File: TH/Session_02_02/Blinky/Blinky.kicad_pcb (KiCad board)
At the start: 2 copper layers, 12 parts, among them U1 TLC551CD‎

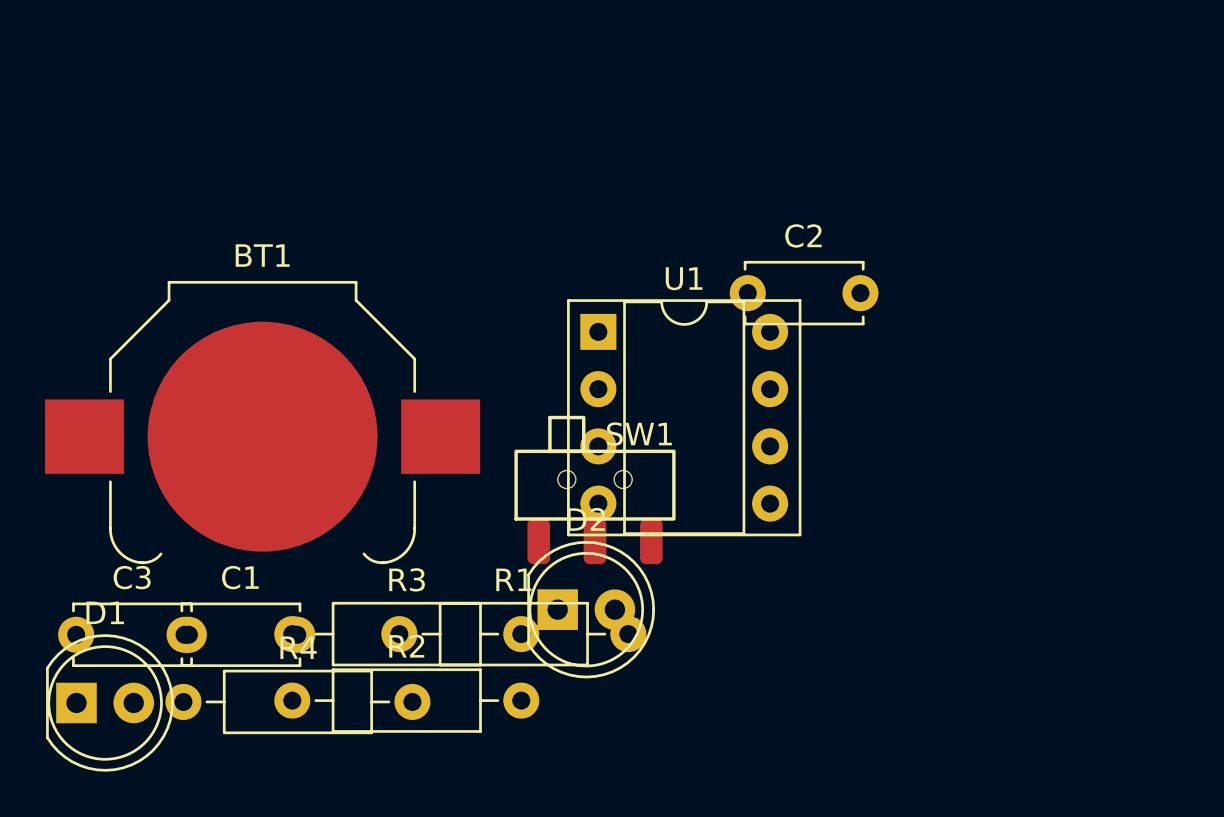
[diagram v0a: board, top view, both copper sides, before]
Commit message: Revamps the through-hole project as transistor based
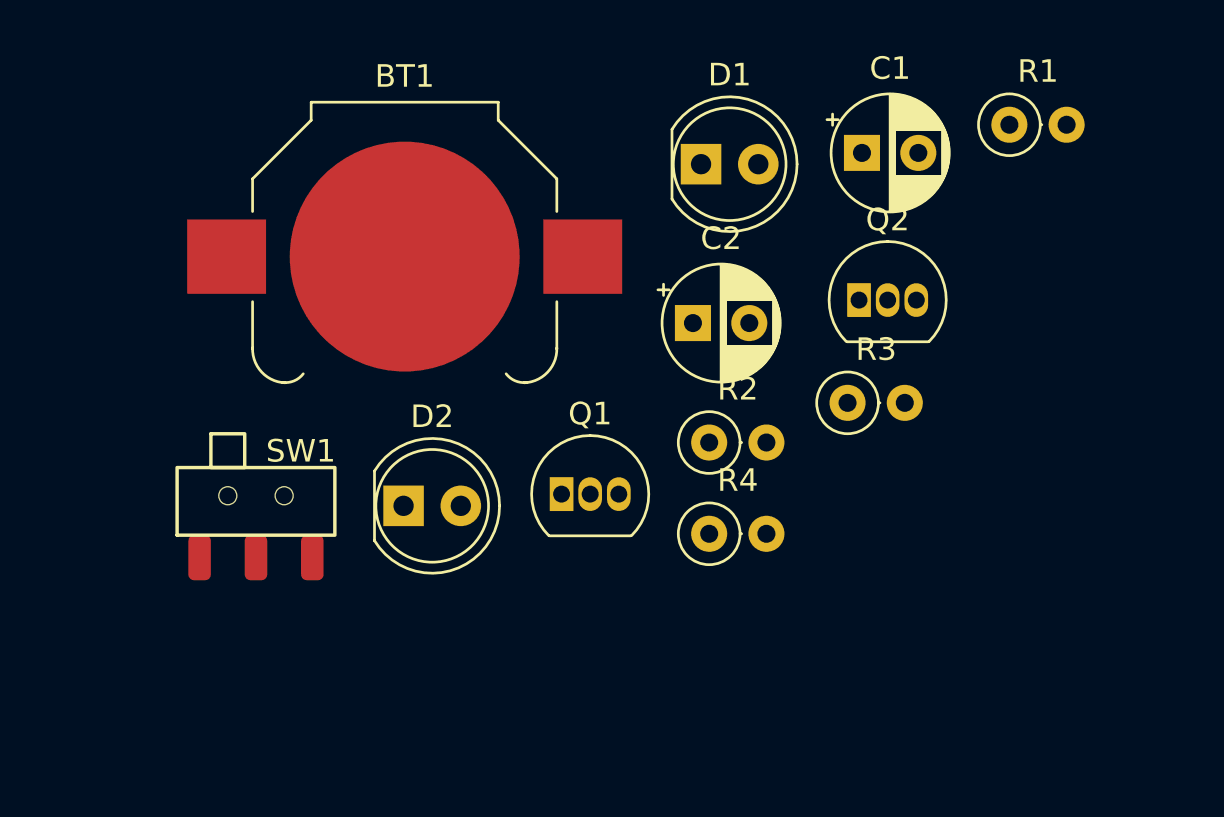
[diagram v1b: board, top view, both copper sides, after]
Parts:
- removed C3: 100nF, Capacitor_THT:C_Disc_D5.0mm_W2.5mm_P5.00mm
- removed SW?: SW_SPDT, Blinky_ZAM:SSK-1202
- removed U1: TLC551CD‎, Package_DIP:DIP-8_W7.62mm_Socket
- added Q1: 2N3904, Package_TO_SOT_THT:TO-92_Inline, F.Cu at (155.0, 98.4)
- added Q2: 2N3904, Package_TO_SOT_THT:TO-92_Inline, F.Cu at (168.2, 89.8)
- added SW1: SW_SPST, Blinky_ZAM:SSK-1202, F.Cu at (141.5, 101.2)
- C1: value 300nF -> 10μF; footprint Capacitor_THT:C_Disc_D5.0mm_W2.5mm_P5.00mm -> Capacitor_THT:CP_Radial_D5.0mm_P2.50mm
- C2: value 100nF -> 10μF; footprint Capacitor_THT:C_Disc_D5.0mm_W2.5mm_P5.00mm -> Capacitor_THT:CP_Radial_D5.0mm_P2.50mm
- R1: value 10kΩ -> 220Ω; footprint Resistor_THT:R_Axial_DIN0207_L6.3mm_D2.5mm_P10.16mm_Horizontal -> Resistor_THT:R_Axial_DIN0207_L6.3mm_D2.5mm_P2.54mm_Vertical
- R2: value 1MΩ -> 100kΩ; footprint Resistor_THT:R_Axial_DIN0207_L6.3mm_D2.5mm_P10.16mm_Horizontal -> Resistor_THT:R_Axial_DIN0207_L6.3mm_D2.5mm_P2.54mm_Vertical
- R3: value 200Ω -> 100kΩ; footprint Resistor_THT:R_Axial_DIN0207_L6.3mm_D2.5mm_P10.16mm_Horizontal -> Resistor_THT:R_Axial_DIN0207_L6.3mm_D2.5mm_P2.54mm_Vertical
- R4: value 200Ω -> 220Ω; footprint Resistor_THT:R_Axial_DIN0207_L6.3mm_D2.5mm_P10.16mm_Horizontal -> Resistor_THT:R_Axial_DIN0207_L6.3mm_D2.5mm_P2.54mm_Vertical
- moved C1 36.9 mm to (168.4, 83.3)
- moved D1 36.6 mm to (161.2, 83.8)
- moved R1 35.3 mm to (174.9, 82.0)
- moved R3 26.7 mm to (167.7, 94.4)
- moved R4 24.5 mm to (161.6, 100.2)
- moved R2 21.8 mm to (161.6, 96.1)
- moved BT1 10.2 mm to (148.1, 87.9)
- moved D2 8.24 mm to (148.0, 98.9)
- moved C2 2.77 mm to (160.9, 90.8)
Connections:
- C1 pad 2: GND -> Net-(C1-Pad2)
- C2 pad 2: GND -> Net-(C2-Pad2)
- D1 pad 1: Net-(D1-Pad1) -> Net-(C1-Pad2)
- D1 pad 2: Net-(C2-Pad1) -> Net-(D1-Pad2)
- D2 pad 1: Net-(D2-Pad1) -> Net-(C2-Pad2)
- R1 pad 1: Net-(C2-Pad1) -> Net-(R1-Pad1)
- R1 pad 2: Net-(R1-Pad2) -> Net-(D1-Pad2)
- R2 pad 1: Net-(R1-Pad2) -> Net-(R1-Pad1)
- R3 pad 1: Net-(D1-Pad1) -> Net-(R1-Pad1)
- R3 pad 2: Net-(D2-Pad2) -> Net-(C2-Pad1)
- R4 pad 1: Net-(D2-Pad1) -> Net-(R1-Pad1)
- R4 pad 2: GND -> Net-(D2-Pad2)

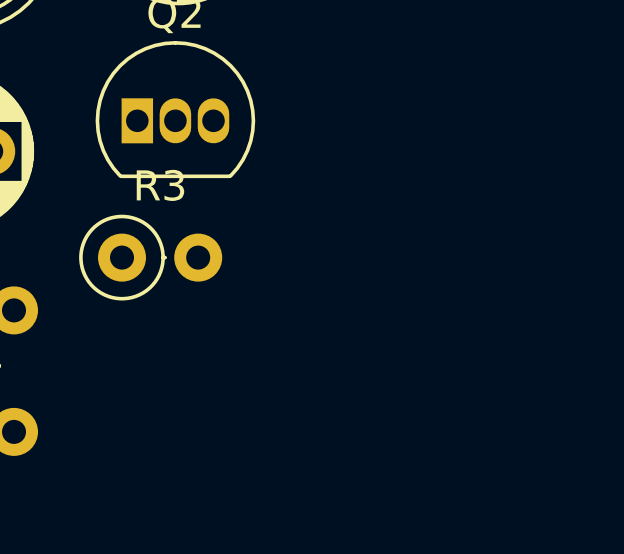
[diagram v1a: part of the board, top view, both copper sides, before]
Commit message: Makes corrections to the design rules
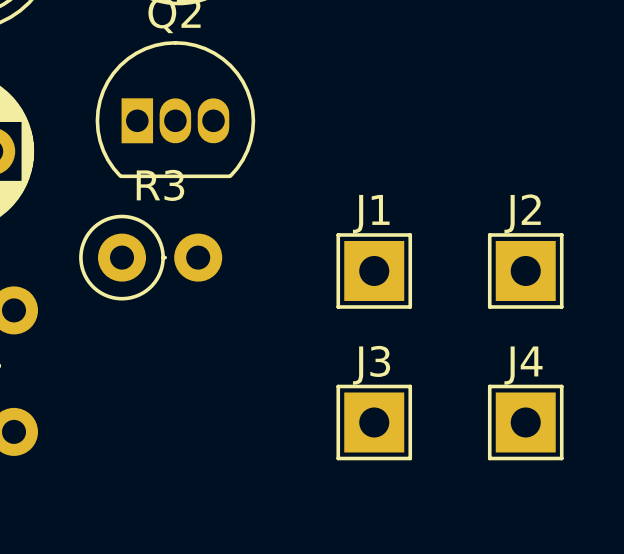
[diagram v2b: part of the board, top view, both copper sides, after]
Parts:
- added J1: Jumper_1, TestPoint:TestPoint_THTPad_2.0x2.0mm_Drill1.0mm, F.Cu at (176.1, 94.8)
- added J2: Jumper_1, TestPoint:TestPoint_THTPad_2.0x2.0mm_Drill1.0mm, F.Cu at (181.2, 94.8)
- added J4: Jumper_1, TestPoint:TestPoint_THTPad_2.0x2.0mm_Drill1.0mm, F.Cu at (181.2, 99.9)
- added J?: Jumper_1, TestPoint:TestPoint_THTPad_2.0x2.0mm_Drill1.0mm, F.Cu at (176.1, 99.9)
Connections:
- Q1 pad 2: Net-(C2-Pad1) -> Net-(J1-Pad1)
- Q2 pad 2: Net-(C1-Pad1) -> Net-(J4-Pad1)
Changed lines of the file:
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@@
     (48 "B.Fab" user)
     (49 "F.Fab" user)
-    (50 "User.1" user)
-    (51 "User.2" user)
-    (52 "User.3" user)
-    (53 "User.4" user)
-    (54 "User.5" user)
-    (55 "User.6" user)
-    (56 "User.7" user)
-    (57 "User.8" user)
-    (58 "User.9" user)
+    (50 "User.1" user "Nutzer.1")
+    (51 "User.2" user "Nutzer.2")
+    (52 "User.3" user "Nutzer.3")
+    (53 "User.4" user "Nutzer.4")
+    (54 "User.5" user "Nutzer.5")
+    (55 "User.6" user "Nutzer.6")
+    (56 "User.7" user "Nutzer.7")
+    (57 "User.8" user "Nutzer.8")
+    (58 "User.9" user "Nutzer.9")
   )
   (setup
+    (stackup
+      (layer "F.SilkS" (type "Top Silk Screen"))
+      (layer "F.Paste" (type "Top Solder Paste"))
+      (layer "F.Mask" (type "Top Solder Mask") (thickness 0.01))
+      (layer "F.Cu" (type "copper") (thickness 0.035))
+      (layer "dielectric 1" (type "core") (thickness 1.51) (material "FR4") (epsilon_r 4.5) (loss_tangent 0.02))
+      (layer "B.Cu" (type "copper") (thickness 0.035))
+      (layer "B.Mask" (type "Bottom Solder Mask") (thickness 0.01))
+      (layer "B.Paste" (type "Bottom Solder Paste"))
+      (layer "B.SilkS" (type "Bottom Silk Screen"))
+      (copper_finish "None")
+      (dielectric_constraints no)
+    )
     (pad_to_mask_clearance 0)
     (pcbplotparams
@@
   (net 8 "Net-(D2-Pad2)")
   (net 9 "Net-(R1-Pad1)")
+  (net 10 "Net-(J1-Pad1)")
+  (net 11 "Net-(J4-Pad1)")
   (footprint "Capacitor_THT:CP_Radial_D5.0mm_P2.50mm" (layer "F.Cu")
     (at 168.371775 83.284)
@@
       (net 2 "GND") (pinfunction "E") (pintype "passive"))
     (pad "2" thru_hole oval (at 1.27 0) (size 1.05 1.5) (drill 0.75) (layers *.Cu *.Mask)
-      (net 4 "Net-(C2-Pad1)") (pinfunction "B") (pintype "passive"))
+      (net 10 "Net-(J1-Pad1)") (pinfunction "B") (pintype "passive"))
     (pad "3" thru_hole oval (at 2.54 0) (size 1.05 1.5) (drill 0.75) (layers *.Cu *.Mask)
       (net 5 "Net-(C1-Pad2)") (pinfunction "C") (pintype "passive"))
@@
     )
   )
+  (footprint "TestPoint:TestPoint_THTPad_2.0x2.0mm_Drill1.0mm" (layer "F.Cu")
+    (at 176.14 99.87)
+    (descr "THT rectangular pad as test Point, square 2.0mm_Drill1.0mm  side length, hole diameter 1.0mm")
+    (tags "test point THT pad rectangle square")
+    (property "Reference" "J?")
+    (property "Sheetfile" "Blinky.kicad_sch")
+    (property "Sheetname" "")
+    (property "Value" "Jumper_1")
+    (attr exclude_from_pos_files)
+    (fp_text reference "J3" (at 0 -1.998) (layer "F.SilkS")
+      (effects (font (size 1 1) (thickness 0.15)))
+    )
+    (fp_text value "Jumper_1" (at 0 2.05) (layer "F.Fab")
+      (effects (font (size 1 1) (thickness 0.15)))
+    )
+    (fp_text user "${REFERENCE}" (at 0 -2) (layer "F.Fab")
+      (effects (font (size 1 1) (thickness 0.15)))
+    )
+    (fp_line (start 1.2 1.2) (end -1.2 1.2) (layer "F.SilkS") (width 0.12))
+    (fp_line (start 1.2 -1.2) (end 1.2 1.2) (layer "F.SilkS") (width 0.12))
+    (fp_line (start -1.2 -1.2) (end 1.2 -1.2) (layer "F.SilkS") (width 0.12))
+    (fp_line (start -1.2 1.2) (end -1.2 -1.2) (layer "F.SilkS") (width 0.12))
+    (fp_line (start 1.5 1.5) (end -1.5 1.5) (layer "F.CrtYd") (width 0.05))
+    (fp_line (start 1.5 1.5) (end 1.5 -1.5) (layer "F.CrtYd") (width 0.05))
+    (fp_line (start -1.5 -1.5) (end 1.5 -1.5) (layer "F.CrtYd") (width 0.05))
+    (fp_line (start -1.5 -1.5) (end -1.5 1.5) (layer "F.CrtYd") (width 0.05))
+    (pad "1" thru_hole rect (at 0 0) (size 2 2) (drill 1) (layers *.Cu *.Mask)
+      (net 4 "Net-(C2-Pad1)") (pintype "unspecified"))
+  )
   (footprint "Resistor_THT:R_Axial_DIN0207_L6.3mm_D2.5mm_P2.54mm_Vertical" (layer "F.Cu")
     (at 174.912 82.034)
@@
       (net 2 "GND") (pinfunction "E") (pintype "passive"))
     (pad "2" thru_hole oval (at 1.27 0) (size 1.05 1.5) (drill 0.75) (layers *.Cu *.Mask)
-      (net 3 "Net-(C1-Pad1)") (pinfunction "B") (pintype "passive"))
+      (net 11 "Net-(J4-Pad1)") (pinfunction "B") (pintype "passive"))
     (pad "3" thru_hole oval (at 2.54 0) (size 1.05 1.5) (drill 0.75) (layers *.Cu *.Mask)
       (net 6 "Net-(C2-Pad2)") (pinfunction "C") (pintype "passive"))
@@
     )
   )
+  (footprint "TestPoint:TestPoint_THTPad_2.0x2.0mm_Drill1.0mm" (layer "F.Cu")
+    (at 181.19 94.82)
+    (descr "THT rectangular pad as test Point, square 2.0mm_Drill1.0mm  side length, hole diameter 1.0mm")
+    (tags "test point THT pad rectangle square")
+    (property "Sheetfile" "Blinky.kicad_sch")
+    (property "Sheetname" "")
+    (attr exclude_from_pos_files)
+    (fp_text reference "J2" (at 0 -1.998) (layer "F.SilkS")
+      (effects (font (size 1 1) (thickness 0.15)))
+    )
+    (fp_text value "Jumper_1" (at 0 2.05) (layer "F.Fab")
+      (effects (font (size 1 1) (thickness 0.15)))
+    )
+    (fp_text user "${REFERENCE}" (at 0 -2) (layer "F.Fab")
+      (effects (font (size 1 1) (thickness 0.15)))
+    )
+    (fp_line (start -1.2 1.2) (end -1.2 -1.2) (layer "F.SilkS") (width 0.12))
+    (fp_line (start 1.2 -1.2) (end 1.2 1.2) (layer "F.SilkS") (width 0.12))
+    (fp_line (start 1.2 1.2) (end -1.2 1.2) (layer "F.SilkS") (width 0.12))
+    (fp_line (start -1.2 -1.2) (end 1.2 -1.2) (layer "F.SilkS") (width 0.12))
+    (fp_line (start -1.5 -1.5) (end 1.5 -1.5) (layer "F.CrtYd") (width 0.05))
+    (fp_line (start 1.5 1.5) (end -1.5 1.5) (layer "F.CrtYd") (width 0.05))
+    (fp_line (start 1.5 1.5) (end 1.5 -1.5) (layer "F.CrtYd") (width 0.05))
+    (fp_line (start -1.5 -1.5) (end -1.5 1.5) (layer "F.CrtYd") (width 0.05))
+    (pad "1" thru_hole rect (at 0 0) (size 2 2) (drill 1) (layers *.Cu *.Mask)
+      (net 3 "Net-(C1-Pad1)") (pintype "unspecified"))
+  )
+  (footprint "TestPoint:TestPoint_THTPad_2.0x2.0mm_Drill1.0mm" (layer "F.Cu")
+    (at 176.14 94.82)
+    (descr "THT rectangular pad as test Point, square 2.0mm_Drill1.0mm  side length, hole diameter 1.0mm")
+    (tags "test point THT pad rectangle square")
+    (property "Sheetfile" "Blinky.kicad_sch")
+    (property "Sheetname" "")
+    (attr exclude_from_pos_files)
+    (fp_text reference "J1" (at 0 -1.998) (layer "F.SilkS")
+      (effects (font (size 1 1) (thickness 0.15)))
+    )
+    (fp_text value "Jumper_1" (at 0 2.05) (layer "F.Fab")
+      (effects (font (size 1 1) (thickness 0.15)))
+    )
+    (fp_text user "${REFERENCE}" (at 0 -2) (layer "F.Fab")
+      (effects (font (size 1 1) (thickness 0.15)))
+    )
+    (fp_line (start -1.2 -1.2) (end 1.2 -1.2) (layer "F.SilkS") (width 0.12))
+    (fp_line (start 1.2 -1.2) (end 1.2 1.2) (layer "F.SilkS") (width 0.12))
+    (fp_line (start -1.2 1.2) (end -1.2 -1.2) (layer "F.SilkS") (width 0.12))
+    (fp_line (start 1.2 1.2) (end -1.2 1.2) (layer "F.SilkS") (width 0.12))
+    (fp_line (start 1.5 1.5) (end -1.5 1.5) (layer "F.CrtYd") (width 0.05))
+    (fp_line (start 1.5 1.5) (end 1.5 -1.5) (layer "F.CrtYd") (width 0.05))
+    (fp_line (start -1.5 -1.5) (end -1.5 1.5) (layer "F.CrtYd") (width 0.05))
+    (fp_line (start -1.5 -1.5) (end 1.5 -1.5) (layer "F.CrtYd") (width 0.05))
+    (pad "1" thru_hole rect (at 0 0) (size 2 2) (drill 1) (layers *.Cu *.Mask)
+      (net 10 "Net-(J1-Pad1)") (pintype "unspecified"))
+  )
+  (footprint "TestPoint:TestPoint_THTPad_2.0x2.0mm_Drill1.0mm" (layer "F.Cu")
+    (at 181.19 99.87)
+    (descr "THT rectangular pad as test Point, square 2.0mm_Drill1.0mm  side length, hole diameter 1.0mm")
+    (tags "test point THT pad rectangle square")
+    (property "Sheetfile" "Blinky.kicad_sch")
+    (property "Sheetname" "")
+    (attr exclude_from_pos_files)
+    (fp_text reference "J4" (at 0 -1.998) (layer "F.SilkS")
+      (effects (font (size 1 1) (thickness 0.15)))
+    )
+    (fp_text value "Jumper_1" (at 0 2.05) (layer "F.Fab")
+      (effects (font (size 1 1) (thickness 0.15)))
+    )
+    (fp_text user "${REFERENCE}" (at 0 -2) (layer "F.Fab")
+      (effects (font (size 1 1) (thickness 0.15)))
+    )
+    (fp_line (start 1.2 -1.2) (end 1.2 1.2) (layer "F.SilkS") (width 0.12))
+    (fp_line (start -1.2 -1.2) (end 1.2 -1.2) (layer "F.SilkS") (width 0.12))
+    (fp_line (start -1.2 1.2) (end -1.2 -1.2) (layer "F.SilkS") (width 0.12))
+    (fp_line (start 1.2 1.2) (end -1.2 1.2) (layer "F.SilkS") (width 0.12))
+    (fp_line (start -1.5 -1.5) (end -1.5 1.5) (layer "F.CrtYd") (width 0.05))
+    (fp_line (start -1.5 -1.5) (end 1.5 -1.5) (layer "F.CrtYd") (width 0.05))
+    (fp_line (start 1.5 1.5) (end 1.5 -1.5) (layer "F.CrtYd") (width 0.05))
+    (fp_line (start 1.5 1.5) (end -1.5 1.5) (layer "F.CrtYd") (width 0.05))
+    (pad "1" thru_hole rect (at 0 0) (size 2 2) (drill 1) (layers *.Cu *.Mask)
+      (net 11 "Net-(J4-Pad1)") (pintype "unspecified"))
+  )
 )

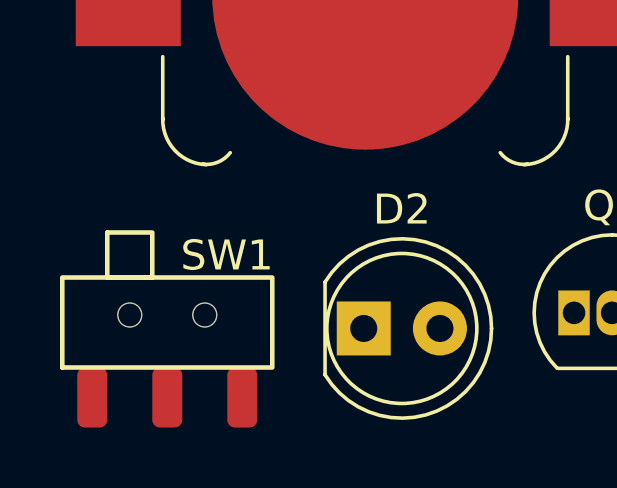
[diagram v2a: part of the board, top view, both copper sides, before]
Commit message: Corrections to the switch footprint
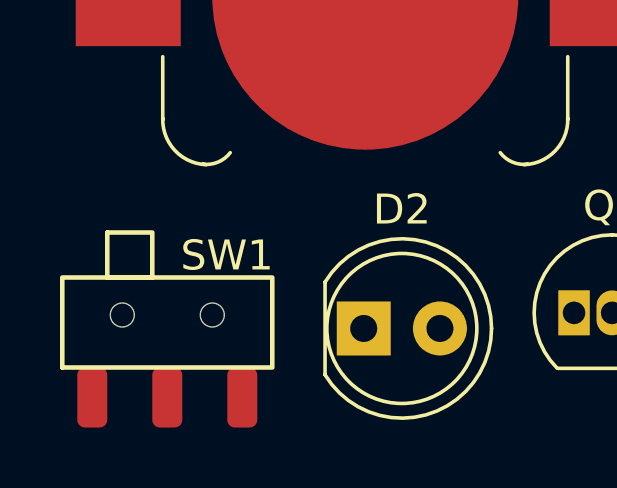
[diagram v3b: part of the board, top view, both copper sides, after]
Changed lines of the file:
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@@
       (effects (font (size 1 1) (thickness 0.15)))
     )
+    (fp_rect (start -2 -5.499999) (end -0.5 -4) (layer "F.SilkS") (width 0.1524) (fill none))
     (fp_rect (start -3.500001 -1) (end 3.500001 -4) (layer "F.SilkS") (width 0.1524) (fill none))
-    (fp_rect (start -2 -5.499999) (end -0.5 -4) (layer "F.SilkS") (width 0.1524) (fill none))
     (fp_rect (start -3.5 -5.5) (end 3.5 1) (layer "F.CrtYd") (width 0.01) (fill none))
-    (pad "" np_thru_hole circle (at 1.25 -2.75) (size 0.8 0.8) (drill 0.8) (layers F&B.Cu *.Mask))
-    (pad "" np_thru_hole circle (at -1.25 -2.75) (size 0.8 0.8) (drill 0.8) (layers F&B.Cu *.Mask))
+    (pad "" np_thru_hole circle (at -1.5 -2.75) (size 0.8 0.8) (drill 0.8) (layers F&B.Cu *.Mask))
+    (pad "" np_thru_hole circle (at 1.5 -2.75) (size 0.8 0.8) (drill 0.8) (layers F&B.Cu *.Mask))
     (pad "1" smd roundrect (at -2.5 0) (size 1 2) (layers "F.Cu" "F.Paste" "F.Mask") (roundrect_rratio 0.25)
       (net 1 "Net-(BT1-Pad1)") (pinfunction "A") (pintype "passive"))
